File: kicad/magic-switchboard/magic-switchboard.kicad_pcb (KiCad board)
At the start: 2 copper layers, 110 x 60 mm, 28 parts, among them M4 MountingHole_4mm, Q1 BC547, Q2 BC547, Q3 BC547, Q4 BC547, SW1 SW_SPST, U1 XY-016

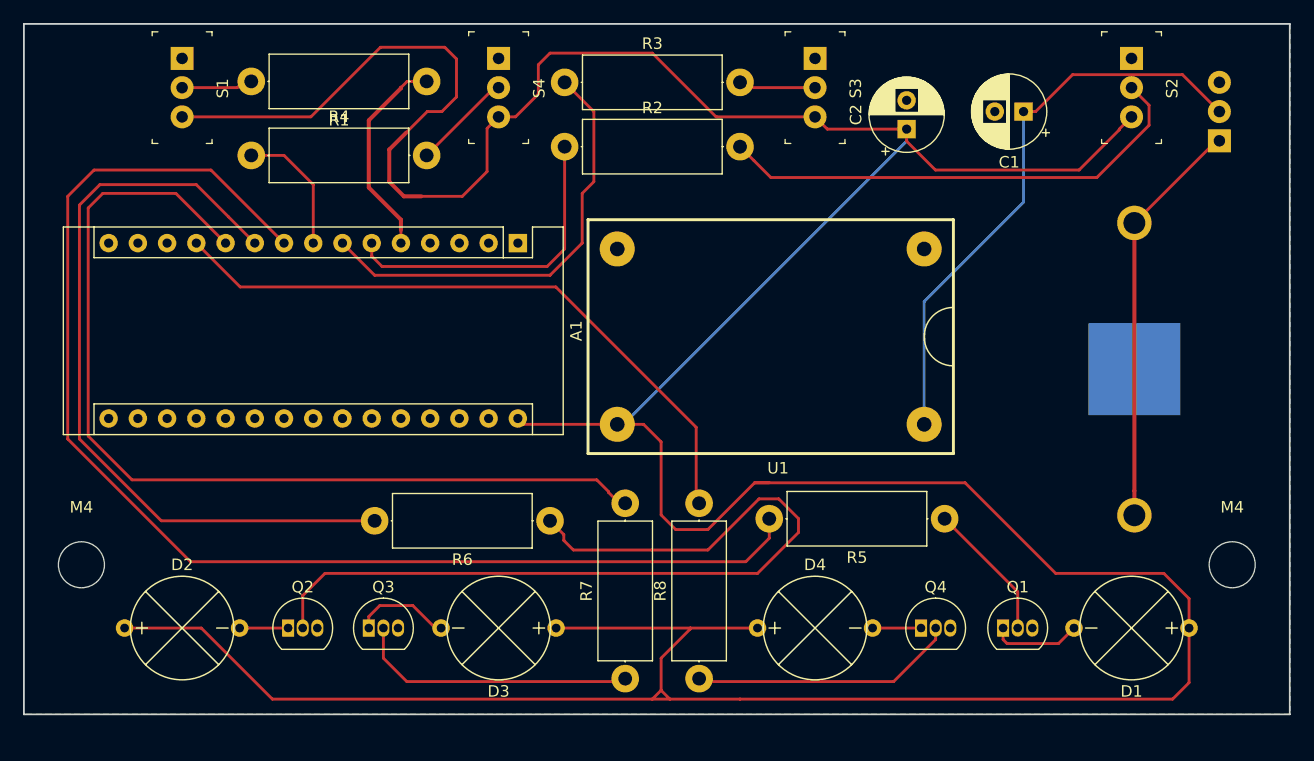
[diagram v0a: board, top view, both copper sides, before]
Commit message: redone pcb v3
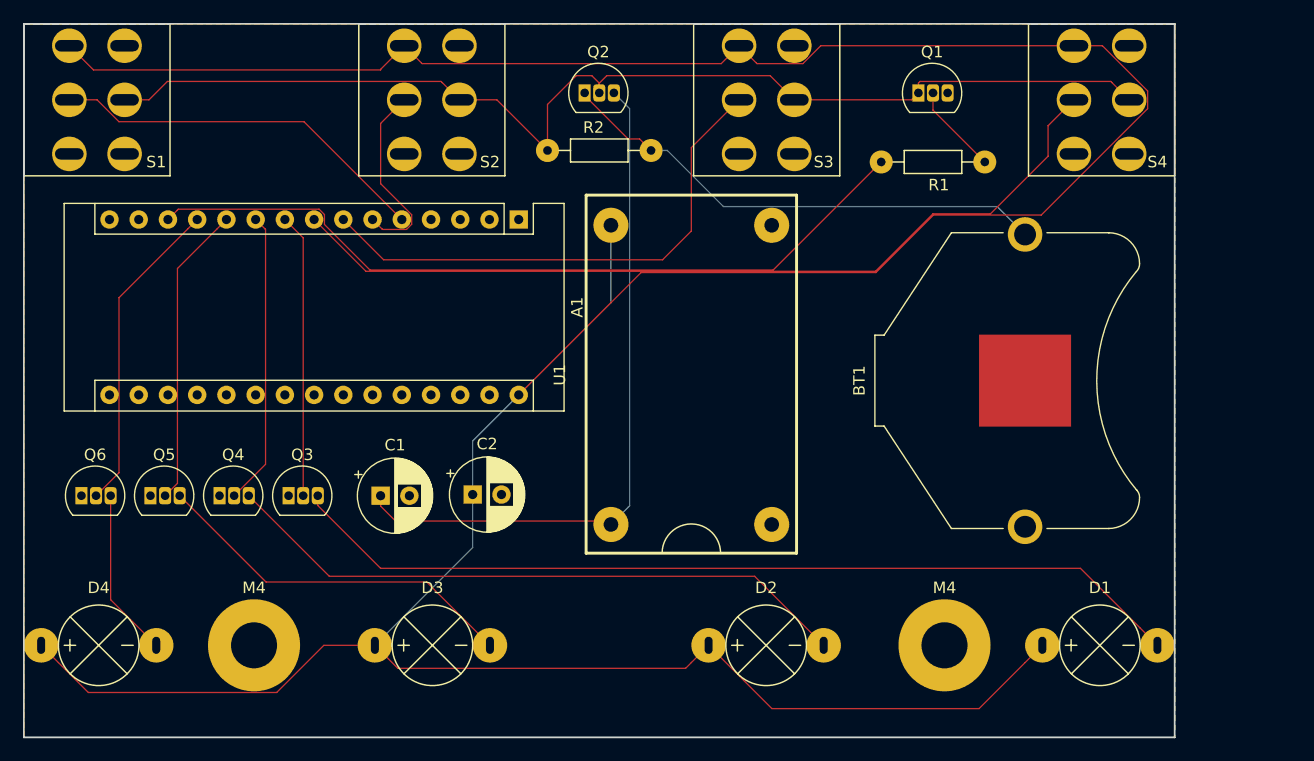
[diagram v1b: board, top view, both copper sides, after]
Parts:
- removed the M4 at (95.0, 127.0)
- removed the M4 at (195.0, 127.0)
- removed R3, R4, R5, R6, R7, R8: 10k, Resistor_THT:R_Axial_DIN0414_L11.9mm_D4.5mm_P15.24mm_Horizontal
- removed SW1: SW_SPST, digikey-footprints:Switch_Toggle_ATE1D-2M3-10-Z
- added M4: MountingHole_4mm_Pad, MountingHole:MountingHole_4mm_Pad, F.Cu at (170.0, 134.0)
- added M4: MountingHole_4mm_Pad, MountingHole:MountingHole_4mm_Pad, F.Cu at (110.0, 134.0)
- added Q5: 2N7000, switchboard:2N700, F.Cu at (101.0, 121.0)
- added Q6: 2N7000, switchboard:2N700, F.Cu at (95.0, 121.0)
- A1: footprint Module:Arduino_Nano -> switchboard:Arduino_Nano
- BT1: footprint Battery:BatteryHolder_Keystone_3009_1x2450 -> switchboard:BatteryHolder_Keystone_3009_1x2450; moved to F.Cu
- C1, C2: footprint Capacitor_THT:CP_Radial_D6.3mm_P2.50mm -> switchboard:CP_Radial_D6.3mm_P2.50mm
- D2: value Green -> Red
- D3: value Blue -> Red
- D4: value Yellow -> Red
- Q1: footprint Package_TO_SOT_THT:TO-92_Inline -> switchboard:BC547
- Q2: value BC547 -> BS250; footprint Package_TO_SOT_THT:TO-92_Inline -> switchboard:BS250
- Q3, Q4: value BC547 -> 2N7000; footprint Package_TO_SOT_THT:TO-92_Inline -> switchboard:2N700
- R1, R2: footprint Resistor_THT:R_Axial_DIN0414_L11.9mm_D4.5mm_P15.24mm_Horizontal -> switchboard:Resistor
- S1, S2, S3, S4: value ATE1D-2M3-10-Z -> MTS-203; footprint digikey-footprints:Switch_Toggle_ATE1D-2M3-10-Z -> switchboard:MTS-203 Switch
- moved C1 65.1 mm to (121.0, 121.0), turned to 0 degrees
- moved D4 62.3 mm to (96.5, 134.0)
- moved Q4 62.0 mm to (107.0, 121.0)
- moved S2 60.8 mm to (125.5, 86.6), turned to 0 degrees
- moved Q2 53.2 mm to (138.7, 86.0)
- moved S4 52.4 mm to (183.7, 86.6), turned to 0 degrees
- moved D2 50.8 mm to (154.5, 134.0)
- moved C2 49.3 mm to (129.0, 120.9), turned to 0 degrees
- moved Q1 47.1 mm to (167.7, 86.0)
- moved R1 44.6 mm to (169.0, 92.0)
- moved Q3 13.4 mm to (113.0, 121.0)
- moved BT1 9.55 mm to (177.0, 111.0), turned to 90 degrees
- moved U1 8.23 mm to (148.0, 110.5), turned to 90 degrees
- moved S1 7.48 mm to (96.3, 86.6), turned to 0 degrees
- moved D3 5.94 mm to (125.5, 134.0), turned to 0 degrees
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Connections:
- A1 pad 13: (no net) -> deadmantrap
- Q1 pad 1: Net-(D1-Pad1) -> powerswitch
- Q2 pad 1: Net-(D2-Pad1) -> Net-(BT1-Pad1)
- Q2 pad 2: Net-(Q2-Pad2) -> powerswitch
- Q2 pad 3: GND -> Net-(C1-Pad1)
- Q3 pad 1: Net-(D3-Pad1) -> GND
- Q3 pad 2: Net-(Q3-Pad2) -> Net-(A1-Pad9)
- Q3 pad 3: GND -> Net-(D1-Pad1)
- Q4 pad 1: Net-(D4-Pad1) -> GND
- Q4 pad 2: Net-(Q4-Pad2) -> Net-(A1-Pad10)
- Q4 pad 3: GND -> Net-(D2-Pad1)
- R1 pad 1: Net-(A1-Pad5) -> Net-(Q1-Pad2)
- R1 pad 2: Net-(R1-Pad2) -> deadmantrap
- R2 pad 1: Net-(A1-Pad6) -> powerswitch
- R2 pad 2: Net-(R2-Pad2) -> Net-(BT1-Pad1)
- S1 pad 1: GND -> VCC
- S1 pad 2: Net-(R1-Pad2) -> Net-(A1-Pad5)
- S1 pad 3: VCC -> GND
- S2 pad 1: GND -> VCC
- S2 pad 2: Net-(R2-Pad2) -> Net-(A1-Pad6)
- S2 pad 3: VCC -> GND
- S3 pad 1: GND -> VCC
- S3 pad 2: Net-(R3-Pad2) -> Net-(A1-Pad7)
- S3 pad 3: VCC -> GND
- S4 pad 1: GND -> VCC
- S4 pad 2: Net-(R4-Pad2) -> Net-(A1-Pad8)
- S4 pad 3: VCC -> GND
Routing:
- net powerswitch: track 0.00 -> 99.6 mm
- net Net-(A1-Pad9): track 111.4 -> 24.7 mm
- net Net-(Q2-Pad2): track 74.9 -> 0.00 mm
- net Net-(D1-Pad1): track 7.86 -> 78.8 mm
- net deadmantrap: track 0.00 -> 68.9 mm
- net Net-(A1-Pad8): track 11.5 -> 75.6 mm
- net Net-(A1-Pad11): track 83.0 -> 26.2 mm
- net VCC: track 359.4 -> 307.5 mm
- net Net-(D2-Pad1): track 3.71 -> 55.3 mm
- net Net-(R2-Pad2): track 42.8 -> 0.00 mm
- net Net-(A1-Pad10): track 67.0 -> 25.5 mm
- net Net-(A1-Pad12): track 56.9 -> 27.6 mm
- net Net-(D3-Pad1): track 7.98 -> 32.3 mm
- net Net-(Q3-Pad2): track 24.2 -> 0.00 mm
- net Net-(Q4-Pad2): track 23.3 -> 0.00 mm
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- added copper zone on F.Cu, net GND
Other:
- board size 110 x 60 mm -> 100 x 62 mm
- net class Default: clearance 0.00254 -> 0.05; trace_width 0.25 -> 0.03
- net class Power added: clearance 0.05, trace_width 0.1, via_dia 0.8, via_drill 0.4
- rule trace_clearance: 0.00254 -> 0.05
- rule trace_min: 0.2 -> 0.02
- board text added: "Magic Switchboard v3"
- board text removed: "Magic Switchboard v2"

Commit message: created gerbers for v3
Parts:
- removed M4 (x2): MountingHole_4mm_Pad, MountingHole:MountingHole_4mm_Pad
- added U2: 5V Boost Converter, switchboard:BoostConverter3Pin, F.Cu at (150.0, 110.5)
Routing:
- net VCC: track 307.5 -> 326.3 mm
- net Net-(C1-Pad1): track 60.2 -> 74.6 mm

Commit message: attiny2313 board
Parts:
- removed A1: Arduino_Nano_v3.x, switchboard:Arduino_Nano
- removed Q5, Q6: 2N7000, switchboard:2N700
- removed S1, S2, S3, S4: MTS-203, switchboard:MTS-203 Switch
- added J1: AVR-ISP-6, switchboard:ISP6, F.Cu at (96.9, 108.1)
- added R3: 10k, switchboard:Resistor, F.Cu at (123.0, 106.0)
- added R4: 10k, switchboard:Resistor, F.Cu at (123.0, 100.0)
- added REF**: MountingHole_4.3mm_M4_DIN965_Pad, MountingHole:MountingHole_4.3mm_M4_DIN965_Pad, F.Cu at (110.0, 134.0)
- added REF**: MountingHole_4.3mm_M4_DIN965_Pad, MountingHole:MountingHole_4.3mm_M4_DIN965_Pad, F.Cu at (170.0, 134.0)
- added SW1: MTS-103, switchboard:MTS-103 Switch, F.Cu at (94.0, 87.0)
- added SW2: MTS-103, switchboard:MTS-103 Switch, F.Cu at (124.7, 87.0)
- added SW3: MTS-103, switchboard:MTS-103 Switch, F.Cu at (155.3, 87.0)
- added SW4: MTS-103, switchboard:MTS-103 Switch, F.Cu at (186.1, 87.0)
- Q1: footprint switchboard:BC547 -> Package_TO_SOT_THT:TO-92_Inline
- Q2: value BS250 -> BC547; footprint switchboard:BS250 -> Package_TO_SOT_THT:TO-92_Inline
- Q3, Q4: value 2N7000 -> BC547; footprint switchboard:2N700 -> Package_TO_SOT_THT:TO-92_Inline
- U1: value XY-016 -> ATtiny2313A-PU; footprint switchboard:XY-016 -> switchboard:ATtiny2313
- U2: value 5V Boost Converter -> 5V Boost
- moved R1 53.1 mm to (122.8, 118.0)
- moved U1 44.5 mm to (104.7, 100.3), turned to 0 degrees
- moved Q1 37.9 mm to (151.0, 120.0)
- moved Q2 34.6 mm to (145.0, 120.0)
- moved C1 34.0 mm to (107.0, 90.0)
- moved R2 27.1 mm to (122.9, 112.0), turned to 180 degrees
- moved Q3 26.0 mm to (139.0, 120.0)
- moved Q4 26.0 mm to (133.0, 120.0)
- moved C2 18.2 mm to (143.2, 109.5)
- moved U2 15.6 mm to (137.5, 101.0), turned to 0 degrees
- moved BT1 1.00 mm to (176.0, 111.0)
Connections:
- BT1 pad 1: Net-(BT1-Pad1) -> VCC
- C1 pad 1: Net-(C1-Pad1) -> VCC
- C2 pad 1: VCC -> +5V
- D1 pad 2: VCC -> +5V
- D2 pad 2: VCC -> +5V
- D3 pad 2: VCC -> +5V
- D4 pad 2: VCC -> +5V
- Q1 pad 1: powerswitch -> Net-(D1-Pad1)
- Q2 pad 1: Net-(BT1-Pad1) -> Net-(D2-Pad1)
- Q2 pad 2: powerswitch -> Net-(Q2-Pad2)
- Q2 pad 3: Net-(C1-Pad1) -> GND
- Q3 pad 1: GND -> Net-(D3-Pad1)
- Q3 pad 3: Net-(D1-Pad1) -> GND
- Q4 pad 1: GND -> Net-(D4-Pad1)
- Q4 pad 3: Net-(D2-Pad1) -> GND
- R1 pad 2: deadmantrap -> Net-(R1-Pad2)
- R2 pad 1: powerswitch -> Net-(Q2-Pad2)
- R2 pad 2: Net-(BT1-Pad1) -> Net-(J1-Pad4)
- U1 pad 1: Net-(C1-Pad1) -> Net-(J1-Pad5)
- U1 pad 2: GND -> (no net)
- U1 pad 3: GND -> (no net)
- U1 pad 4: VCC -> (no net)
- U2 pad 1: Net-(C1-Pad1) -> VCC
- U2 pad 3: VCC -> +5V
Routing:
- net +5V: track 0.00 -> 133.2 mm
- net VCC: track 326.3 -> 205.2 mm
- net Net-(SW4-Pad2): track 0.00 -> 112.0 mm
- net powerswitch: track 99.6 -> 0.00 mm
- net Net-(SW3-Pad2): track 0.00 -> 79.5 mm
- net Net-(A1-Pad8): track 75.6 -> 0.00 mm
- net Net-(C1-Pad1): track 74.6 -> 0.00 mm
- net deadmantrap: track 68.9 -> 0.00 mm
- net Net-(SW1-Pad2): track 0.00 -> 52.9 mm
- net Net-(A1-Pad7): track 45.8 -> 0.00 mm
- net Net-(SW2-Pad2): track 0.00 -> 43.5 mm
- net Net-(BT1-Pad1): track 43.5 -> 0.00 mm
- net Net-(Q1-Pad2): track 7.86 -> 48.0 mm
- net Net-(D1-Pad1): track 78.8 -> 43.4 mm
- net Net-(D2-Pad1): track 55.3 -> 21.2 mm
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- removed copper zone on F.Cu, net GND
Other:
- net class Default: trace_width 0.03 -> 0.1
- net class Power removed
- board text added: "Magic Switchboard v4"
- board text removed: "Magic Switchboard v3"

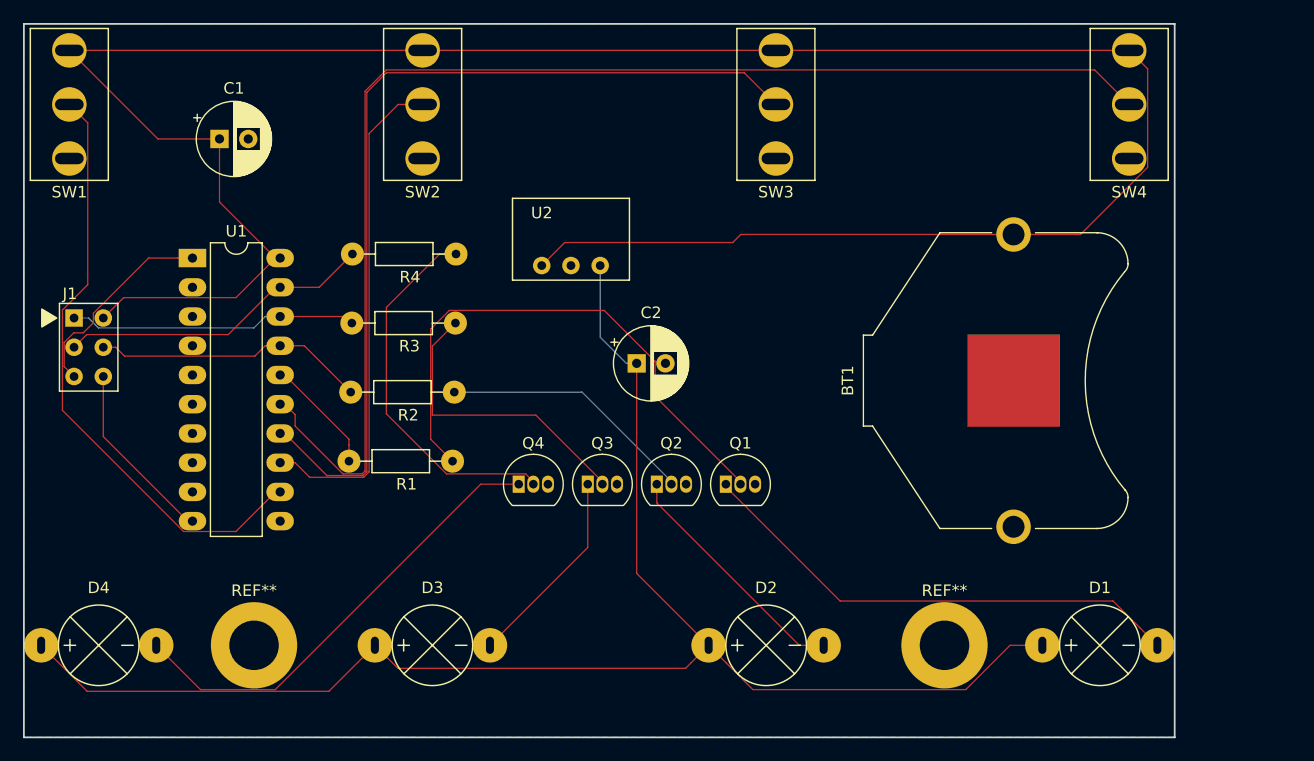
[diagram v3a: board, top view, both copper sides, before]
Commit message: aufgeräumt für v4 (attiny4313)
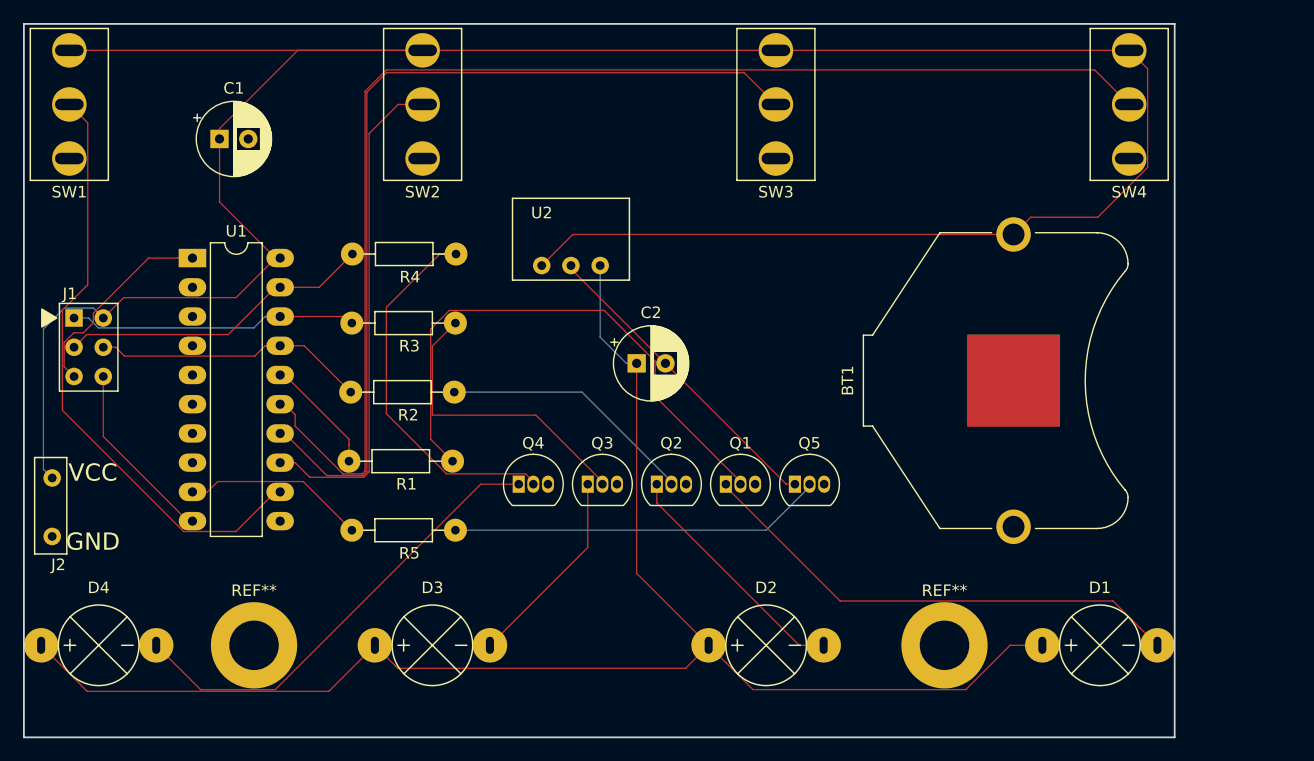
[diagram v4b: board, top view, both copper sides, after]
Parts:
- added J2: Screw_Terminal_01x02, switchboard:ScrewTerminal1x2, F.Cu at (95.0, 122.0)
- added Q5: BC547, Package_TO_SOT_THT:TO-92_Inline, F.Cu at (157.0, 120.0)
- added R5: 10k, switchboard:Resistor, F.Cu at (123.0, 124.0)
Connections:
- C2 pad 2: GND -> Net-(C2-Pad2)
- U1 pad 9: (no net) -> lightpower
- U2 pad 2: GND -> Net-(C2-Pad2)
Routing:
- net Net-(Q5-Pad2): track 0.00 -> 32.6 mm
- net Net-(C2-Pad2): track 0.00 -> 27.5 mm
- net VCC: track 205.2 -> 229.9 mm
- net lightpower: track 0.00 -> 16.0 mm
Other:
- board text added: "GND"
- board text added: "VCC"
